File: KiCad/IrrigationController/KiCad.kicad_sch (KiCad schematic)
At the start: 114 parts, among them IC1 MCP23017-E_SO, IC2 MCP23017-E_SO, IC3 DS89C21TMX_NOPB, J1 Screw_Terminal_01x03, J10 Screw_Terminal_01x05, J11 Screw_Terminal_01x02, J12 Screw_Terminal_01x02, J13 Screw_Terminal_01x04, J14 Screw_Terminal_01x02, J15 Screw_Terminal_01x02, J16 Screw_Terminal_01x02, J17 Screw_Terminal_01x02, J18 Screw_Terminal_01x02, J19 Screw_Terminal_01x02, J2 Screw_Terminal_01x03, J21 Screw_Terminal_01x06, J3 Screw_Terminal_01x03, J4 Conn_01x04_Pin, J5 Screw_Terminal_01x03, J6 Screw_Terminal_01x02, J7 Screw_Terminal_01x02, J8 Screw_Terminal_01x02, J9 Screw_Terminal_01x02, K1 2071556-9, K2 2071556-9, Q1 MMBT3906, Q11 MMBT3904, Q12 MMBT3904, Q2 MMBT3906, Q3 MMBT3906, Q6 MMBT3904, Q7 MMBT3904, Q8 MMBT3904, SW1 SW_Push, U1 L298P, U2 ARDUINO_MKR_WAN_1310, U3 L298P, U4 L298P, U5 L298P, U7 L7805

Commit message: pcb rev1
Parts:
- removed C15: 100n, Capacitor_SMD:C_1206_3216Metric, symbol Device:C
- removed J4: Conn_01x04_Pin, Connector_PinHeader_2.54mm:PinHeader_1x04_P2.54mm_Vertical, symbol Connector:Conn_01x04_Pin
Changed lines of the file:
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@@
     (stroke (width 0) (type default))
   )
-  (wire (pts (xy 394.97 106.68) (xy 394.97 111.76))
-    (stroke (width 0) (type default))
-  )
   (wire (pts (xy 299.72 152.4) (xy 300.99 152.4))
     (stroke (width 0) (type default))
@@
     (stroke (width 0) (type default))
   )
-  (wire (pts (xy 392.43 106.68) (xy 392.43 111.76))
-    (stroke (width 0) (type default))
-  )
   (wire (pts (xy 91.44 185.42) (xy 91.44 200.66))
     (stroke (width 0) (type default))
@@
     (effects (font (size 1.27 1.27)) (justify left bottom))
   )
-  (label "RX" (at 392.43 111.76 90) (fields_autoplaced)
-    (effects (font (size 1.27 1.27)) (justify left bottom))
-  )
   (label "D0-" (at 304.8 36.83 90) (fields_autoplaced)
     (effects (font (size 1.27 1.27)) (justify left bottom))
@@
     (effects (font (size 1.27 1.27)) (justify right bottom))
   )
-  (label "TX" (at 394.97 111.76 90) (fields_autoplaced)
-    (effects (font (size 1.27 1.27)) (justify left bottom))
-  )
   (label "S_ANEM_IN" (at 110.49 46.99 0) (fields_autoplaced)
     (effects (font (size 1.27 1.27)) (justify left bottom))
@@
     (effects (font (size 1.27 1.27)) (justify left bottom))
   )
-  (label "Vin" (at 250.19 20.32 0) (fields_autoplaced)
-    (effects (font (size 1.27 1.27)) (justify left bottom))
-  )
   (label "P5_EN" (at 195.58 132.08 90) (fields_autoplaced)
     (effects (font (size 1.27 1.27)) (justify left bottom))
@@
     )
   )
-  (symbol (lib_id "Device:C") (at 250.19 24.13 180) (unit 1)
-    (in_bom yes) (on_board yes) (dnp no)
-    (property "Reference" "C15" (at 247.65 21.59 0)
-      (effects (font (size 1.27 1.27)))
-    )
-    (property "Value" "100n" (at 254 26.67 0)
-      (effects (font (size 1.27 1.27)))
-    )
-    (property "Footprint" "Capacitor_SMD:C_1206_3216Metric" (at 249.2248 20.32 0)
-      (effects (font (size 1.27 1.27)) hide)
-    )
-    (property "Datasheet" "~" (at 250.19 24.13 0)
-      (effects (font (size 1.27 1.27)) hide)
-    )
-    (property "Mouser Part Number" "80-C1206C334K1RECAUT" (at 250.19 24.13 0)
-      (effects (font (size 1.27 1.27)) hide)
-    )
-    (pin "1")
-    (pin "2")
-    (instances
-      (project "KiCad"
-        (path "/557850ac-a946-4dff-8187-8978353577df"
-          (reference "C15") (unit 1)
-        )
-      )
-    )
-  )
   (symbol (lib_id "power:Earth") (at 33.02 127 0) (mirror y) (unit 1)
     (in_bom yes) (on_board yes) (dnp no) (fields_autoplaced)
@@
     )
   )
-  (symbol (lib_id "power:Earth") (at 250.19 27.94 0) (mirror y) (unit 1)
-    (in_bom yes) (on_board yes) (dnp no) (fields_autoplaced)
-    (property "Reference" "#PWR028" (at 250.19 34.29 0)
-      (effects (font (size 1.27 1.27)) hide)
-    )
-    (property "Value" "Earth" (at 250.19 31.75 0)
-      (effects (font (size 1.27 1.27)) hide)
-    )
-    (property "Footprint" "" (at 250.19 27.94 0)
-      (effects (font (size 1.27 1.27)) hide)
-    )
-    (property "Datasheet" "~" (at 250.19 27.94 0)
-      (effects (font (size 1.27 1.27)) hide)
-    )
-    (pin "1")
-    (instances
-      (project "KiCad"
-        (path "/557850ac-a946-4dff-8187-8978353577df"
-          (reference "#PWR028") (unit 1)
-        )
-      )
-    )
-  )
   (symbol (lib_id "Transistor_BJT:2N3904") (at 210.82 271.78 0) (unit 1)
     (in_bom yes) (on_board yes) (dnp no)
@@
     )
   )
-  (symbol (lib_id "Connector:Conn_01x04_Pin") (at 394.97 101.6 270) (unit 1)
-    (in_bom yes) (on_board yes) (dnp no) (fields_autoplaced)
-    (property "Reference" "J4" (at 393.7 96.52 90)
-      (effects (font (size 1.27 1.27)))
-    )
-    (property "Value" "Conn_01x04_Pin" (at 393.7 99.06 90)
-      (effects (font (size 1.27 1.27)))
-    )
-    (property "Footprint" "Connector_PinHeader_2.54mm:PinHeader_1x04_P2.54mm_Vertical" (at 394.97 101.6 0)
-      (effects (font (size 1.27 1.27)) hide)
-    )
-    (property "Datasheet" "~" (at 394.97 101.6 0)
-      (effects (font (size 1.27 1.27)) hide)
-    )
-    (pin "4")
-    (pin "2")
-    (pin "3")
-    (pin "1")
-    (instances
-      (project "KiCad"
-        (path "/557850ac-a946-4dff-8187-8978353577df"
-          (reference "J4") (unit 1)
-        )
-      )
-    )
-  )
   (symbol (lib_name "+3.3V_1") (lib_id "power:+3.3V") (at 46.99 162.56 0) (unit 1)
     (in_bom yes) (on_board yes) (dnp no) (fields_autoplaced)
@@
     )
   )
-  (symbol (lib_name "+5V_2") (lib_id "power:+5V") (at 389.89 106.68 0) (mirror x) (unit 1)
-    (in_bom yes) (on_board yes) (dnp no) (fields_autoplaced)
-    (property "Reference" "#PWR030" (at 389.89 102.87 0)
-      (effects (font (size 1.27 1.27)) hide)
-    )
-    (property "Value" "+5V" (at 389.89 111.76 0)
-      (effects (font (size 1.27 1.27)))
-    )
-    (property "Footprint" "" (at 389.89 106.68 0)
-      (effects (font (size 1.27 1.27)) hide)
-    )
-    (property "Datasheet" "" (at 389.89 106.68 0)
-      (effects (font (size 1.27 1.27)) hide)
-    )
-    (pin "1")
-    (instances
-      (project "KiCad"
-        (path "/557850ac-a946-4dff-8187-8978353577df"
-          (reference "#PWR030") (unit 1)
-        )
-      )
-    )
-  )
   (symbol (lib_id "power:Earth") (at 237.49 187.96 0) (unit 1)
     (in_bom yes) (on_board yes) (dnp no) (fields_autoplaced)
@@
         )
       )
-    )
-  )
-  (symbol (lib_id "power:Earth") (at 397.51 106.68 0) (mirror y) (unit 1)
-    (in_bom yes) (on_board yes) (dnp no) (fields_autoplaced)
-    (property "Reference" "#PWR032" (at 397.51 113.03 0)
-      (effects (font (size 1.27 1.27)) hide)
-    )
-    (property "Value" "Earth" (at 397.51 110.49 0)
-      (effects (font (size 1.27 1.27)) hide)
-    )
-    (property "Footprint" "" (at 397.51 106.68 0)
-      (effects (font (size 1.27 1.27)) hide)
-    )
-    (property "Datasheet" "~" (at 397.51 106.68 0)
-      (effects (font (size 1.27 1.27)) hide)
-    )
-    (pin "1")
-    (instances
-      (project "KiCad"
-        (path "/557850ac-a946-4dff-8187-8978353577df"
-          (reference "#PWR032") (unit 1)
-        )
-      )

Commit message: qwer
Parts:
- C1, C10, C11, C12, C13, C2, C3, C4, C5, C6, C7, C8, C9: Mouser Part Number 80-C1206C104J4GAUTO -> 80-C1206X104K1RAUTO
- C14: Mouser Part Number 80-C1206C334K1RECAUT -> 80-C1206X334K1RAUTO
- C16, C17, C18: value 100n -> 0.1u; Mouser Part Number 80-C1206C334K1RECAUT -> 80-C1206X104K1RAUTO
- U1, U3, U4, U5: Mouser Part Number (none) -> 511-L298P
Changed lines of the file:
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@@
       (effects (font (size 1.27 1.27)) hide)
     )
-    (property "Mouser Part Number" "80-C1206C104J4GAUTO" (at 275.59 147.32 0)
+    (property "Mouser Part Number" "80-C1206X104K1RAUTO" (at 275.59 147.32 0)
       (effects (font (size 1.27 1.27)) hide)
     )
@@
       (effects (font (size 1.27 1.27)))
     )
-    (property "Value" "100n" (at 265.43 21.59 0)
+    (property "Value" "0.1u" (at 265.43 21.59 0)
       (effects (font (size 1.27 1.27)))
     )
@@
       (effects (font (size 1.27 1.27)) hide)
     )
-    (property "Mouser Part Number" "80-C1206C334K1RECAUT" (at 269.24 24.13 0)
+    (property "Mouser Part Number" "80-C1206X104K1RAUTO" (at 269.24 24.13 0)
       (effects (font (size 1.27 1.27)) hide)
     )
@@
       (effects (font (size 1.27 1.27)) hide)
     )
-    (property "Mouser Part Number" "80-C1206C104J4GAUTO" (at 105.41 184.15 0)
+    (property "Mouser Part Number" "80-C1206X104K1RAUTO" (at 105.41 184.15 0)
       (effects (font (size 1.27 1.27)) hide)
     )
@@
       (effects (font (size 1.27 1.27)) hide)
     )
-    (property "Mouser Part Number" "80-C1206C104J4GAUTO" (at 302.26 184.15 0)
+    (property "Mouser Part Number" "80-C1206X104K1RAUTO" (at 302.26 184.15 0)
       (effects (font (size 1.27 1.27)) hide)
     )
@@
       (effects (font (size 1.27 1.27)) hide)
     )
-    (property "Mouser Part Number" "80-C1206C104J4GAUTO" (at 138.43 184.15 0)
+    (property "Mouser Part Number" "80-C1206X104K1RAUTO" (at 138.43 184.15 0)
       (effects (font (size 1.27 1.27)) hide)
     )
@@
       (effects (font (size 1.27 1.27)) hide)
     )
-    (pin "5")
-    (pin "3")
-    (pin "13")
-    (pin "4")
-    (pin "6")
+    (property "Mouser Part Number" "511-L298P" (at 318.77 152.4 0)
+      (effects (font (size 1.27 1.27)) hide)
+    )
+    (pin "1")
     (pin "10")
-    (pin "2")
-    (pin "16")
-    (pin "8")
-    (pin "18")
     (pin "11")
-    (pin "17")
     (pin "12")
-    (pin "1")
-    (pin "9")
+    (pin "13")
     (pin "14")
-    (pin "7")
     (pin "15")
+    (pin "16")
+    (pin "17")
+    (pin "18")
     (pin "19")
+    (pin "2")
     (pin "20")
+    (pin "3")
+    (pin "4")
+    (pin "5")
+    (pin "6")
+    (pin "7")
+    (pin "8")
+    (pin "9")
     (instances
       (project "KiCad"
@@
       (effects (font (size 1.27 1.27)) hide)
     )
-    (property "Mouser Part Number" "80-C1206C104J4GAUTO" (at 143.51 147.32 0)
+    (property "Mouser Part Number" "80-C1206X104K1RAUTO" (at 143.51 147.32 0)
       (effects (font (size 1.27 1.27)) hide)
     )
@@
       (effects (font (size 1.27 1.27)) hide)
     )
-    (property "Mouser Part Number" "80-C1206C104J4GAUTO" (at 270.51 184.15 0)
+    (property "Mouser Part Number" "80-C1206X104K1RAUTO" (at 270.51 184.15 0)
       (effects (font (size 1.27 1.27)) hide)
     )
@@
       (effects (font (size 1.27 1.27)) hide)
     )
-    (pin "5")
-    (pin "3")
-    (pin "13")
-    (pin "4")
-    (pin "6")
+    (property "Mouser Part Number" "511-L298P" (at 121.92 152.4 0)
+      (effects (font (size 1.27 1.27)) hide)
+    )
+    (pin "1")
     (pin "10")
-    (pin "2")
-    (pin "16")
-    (pin "8")
-    (pin "18")
     (pin "11")
-    (pin "17")
     (pin "12")
-    (pin "1")
-    (pin "9")
+    (pin "13")
     (pin "14")
-    (pin "7")
     (pin "15")
+    (pin "16")
+    (pin "17")
+    (pin "18")
     (pin "19")
+    (pin "2")
     (pin "20")
+    (pin "3")
+    (pin "4")
+    (pin "5")
+    (pin "6")
+    (pin "7")
+    (pin "8")
+    (pin "9")
     (instances
       (project "KiCad"
@@
       (effects (font (size 1.27 1.27)))
     )
-    (property "Value" "100n" (at 273.05 21.59 0)
+    (property "Value" "0.1u" (at 273.05 21.59 0)
       (effects (font (size 1.27 1.27)))
     )
@@
       (effects (font (size 1.27 1.27)) hide)
     )
-    (property "Mouser Part Number" "80-C1206C334K1RECAUT" (at 276.86 24.13 0)
+    (property "Mouser Part Number" "80-C1206X104K1RAUTO" (at 276.86 24.13 0)
       (effects (font (size 1.27 1.27)) hide)
     )
@@
       (effects (font (size 1.27 1.27)) hide)
     )
-    (property "Mouser Part Number" "80-C1206C104J4GAUTO" (at 340.36 147.32 0)
+    (property "Mouser Part Number" "80-C1206X104K1RAUTO" (at 340.36 147.32 0)
       (effects (font (size 1.27 1.27)) hide)
     )
@@
       (effects (font (size 1.27 1.27)) hide)
     )
-    (property "Mouser Part Number" "80-C1206C104J4GAUTO" (at 335.28 184.15 0)
+    (property "Mouser Part Number" "80-C1206X104K1RAUTO" (at 335.28 184.15 0)
       (effects (font (size 1.27 1.27)) hide)
     )
@@
       (effects (font (size 1.27 1.27)) hide)
     )
-    (property "Mouser Part Number" "80-C1206C104J4GAUTO" (at 237.49 184.15 0)
+    (property "Mouser Part Number" "80-C1206X104K1RAUTO" (at 237.49 184.15 0)
       (effects (font (size 1.27 1.27)) hide)
     )
@@
       (effects (font (size 1.27 1.27)) hide)
     )
-    (property "Mouser Part Number" "80-C1206C334K1RECAUT" (at 400.05 68.58 0)
+    (property "Mouser Part Number" "80-C1206X334K1RAUTO" (at 400.05 68.58 0)
       (effects (font (size 1.27 1.27)) hide)
     )
@@
       (effects (font (size 1.27 1.27)))
     )
-    (property "Value" "100n" (at 257.81 21.59 0)
+    (property "Value" "0.1u" (at 257.81 21.59 0)
       (effects (font (size 1.27 1.27)))
     )
@@
       (effects (font (size 1.27 1.27)) hide)
     )
-    (property "Mouser Part Number" "80-C1206C334K1RECAUT" (at 261.62 24.13 0)
+    (property "Mouser Part Number" "80-C1206X104K1RAUTO" (at 261.62 24.13 0)
       (effects (font (size 1.27 1.27)) hide)
     )
@@
       (effects (font (size 1.27 1.27)) hide)
     )
-    (pin "5")
-    (pin "3")
-    (pin "13")
-    (pin "4")
-    (pin "6")
+    (property "Mouser Part Number" "511-L298P" (at 254 152.4 0)
+      (effects (font (size 1.27 1.27)) hide)
+    )
+    (pin "1")
     (pin "10")
-    (pin "2")
-    (pin "16")
-    (pin "8")
-    (pin "18")
     (pin "11")
-    (pin "17")
     (pin "12")
-    (pin "1")
-    (pin "9")
+    (pin "13")
     (pin "14")
-    (pin "7")
     (pin "15")
+    (pin "16")
+    (pin "17")
+    (pin "18")
     (pin "19")
+    (pin "2")
     (pin "20")
+    (pin "3")
+    (pin "4")
+    (pin "5")
+    (pin "6")
+    (pin "7")
+    (pin "8")
+    (pin "9")
     (instances
       (project "KiCad"
@@
       (effects (font (size 1.27 1.27)) hide)
     )
-    (pin "5")
-    (pin "3")
-    (pin "13")
-    (pin "4")
-    (pin "6")
+    (property "Mouser Part Number" "511-L298P" (at 187.96 152.4 0)
+      (effects (font (size 1.27 1.27)) hide)
+    )
+    (pin "1")
     (pin "10")
-    (pin "2")
-    (pin "16")
-    (pin "8")
-    (pin "18")
     (pin "11")
-    (pin "17")
     (pin "12")
-    (pin "1")
-    (pin "9")
+    (pin "13")
     (pin "14")
-    (pin "7")
     (pin "15")
+    (pin "16")
+    (pin "17")
+    (pin "18")
     (pin "19")
+    (pin "2")
     (pin "20")
+    (pin "3")
+    (pin "4")
+    (pin "5")
+    (pin "6")
+    (pin "7")
+    (pin "8")
+    (pin "9")
     (instances
       (project "KiCad"
@@
       (effects (font (size 1.27 1.27)) hide)
     )
-    (property "Mouser Part Number" "80-C1206C104J4GAUTO" (at 171.45 184.15 0)
+    (property "Mouser Part Number" "80-C1206X104K1RAUTO" (at 171.45 184.15 0)
       (effects (font (size 1.27 1.27)) hide)
     )
@@
       (effects (font (size 1.27 1.27)) hide)
     )
-    (property "Mouser Part Number" "80-C1206C104J4GAUTO" (at 204.47 184.15 0)
+    (property "Mouser Part Number" "80-C1206X104K1RAUTO" (at 204.47 184.15 0)
       (effects (font (size 1.27 1.27)) hide)
     )
@@
       (effects (font (size 1.27 1.27)) hide)
     )
-    (property "Mouser Part Number" "80-C1206C104J4GAUTO" (at 398.78 87.63 0)
+    (property "Mouser Part Number" "80-C1206X104K1RAUTO" (at 398.78 87.63 0)
       (effects (font (size 1.27 1.27)) hide)
     )
@@
       (effects (font (size 1.27 1.27)) hide)
     )
-    (property "Mouser Part Number" "80-C1206C104J4GAUTO" (at 209.55 147.32 0)
+    (property "Mouser Part Number" "80-C1206X104K1RAUTO" (at 209.55 147.32 0)
       (effects (font (size 1.27 1.27)) hide)
     )

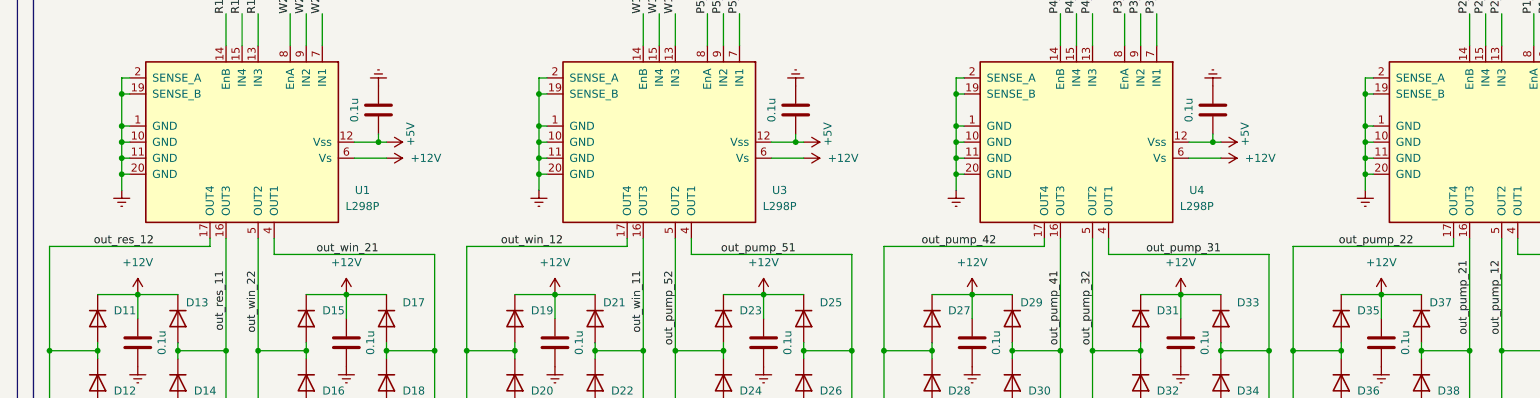
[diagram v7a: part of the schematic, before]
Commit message: Arregladas las conexiones al plano de masa
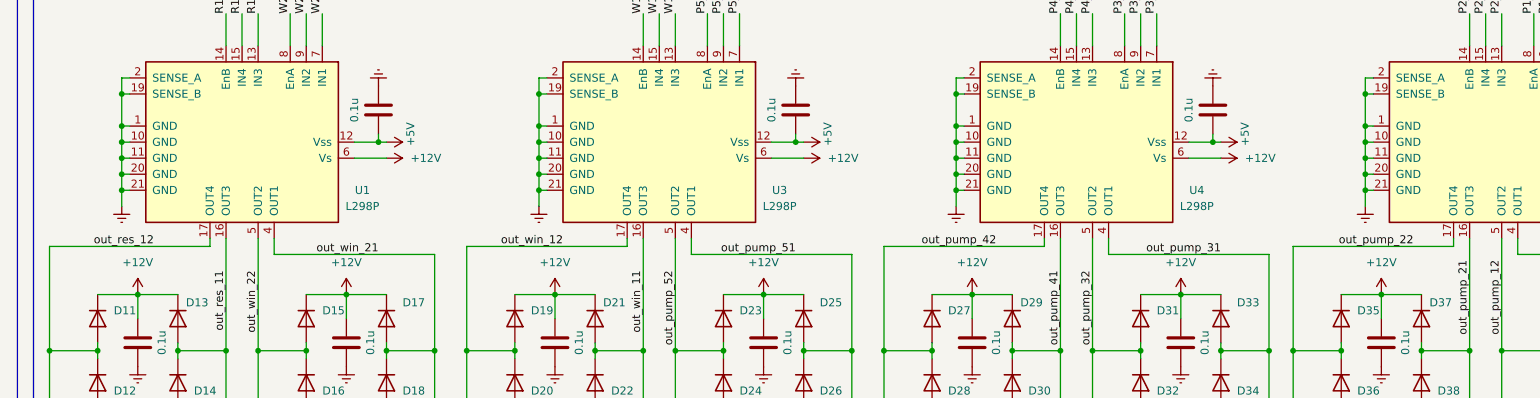
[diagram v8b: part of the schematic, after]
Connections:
- net Earth: now also U1.21 (GND), U3.21 (GND), U4.21 (GND), U5.21 (GND)
